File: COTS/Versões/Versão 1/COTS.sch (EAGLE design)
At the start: 12 parts

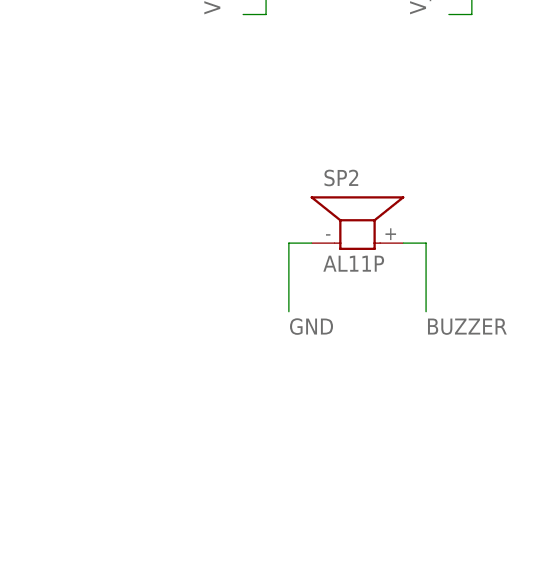
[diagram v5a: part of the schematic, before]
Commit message: CHORE: colocando  pads ovais
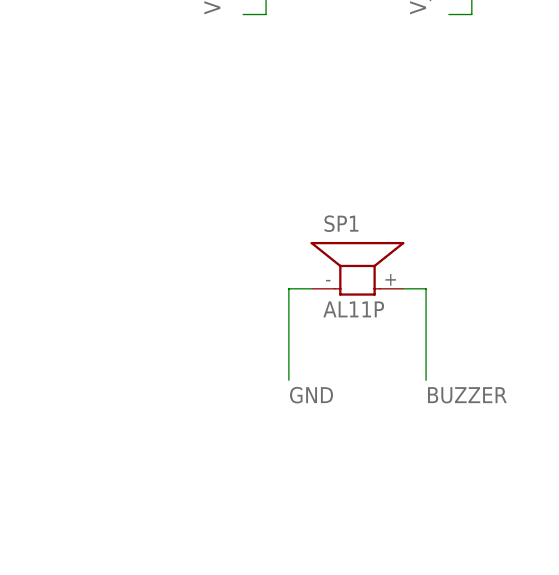
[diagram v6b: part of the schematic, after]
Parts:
- removed SP2: AL11P, buzzer:AL11P
- added SP1: AL11P, buzzer:AL11P
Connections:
- net BUZZER: now also SP1.2; no longer SP2.2
- net GND: now also SP1.1; no longer SP2.1
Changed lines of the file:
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@@
 <drawing>
 <settings>
-<setting alwaysvectorfont="yes"/>
+<setting alwaysvectorfont="no"/>
 <setting verticaltext="up"/>
 </settings>
@@
 </classes>
 <parts>
-<part name="U$1" library="CRD" library_urn="urn:adsk.eagle:library:39051337" deviceset="MPU6050" device="V1" package3d_urn="urn:adsk.eagle:package:39029071/8" override_package3d_urn="urn:adsk.eagle:package:49473311/2" override_package_urn="urn:adsk.eagle:footprint:39029067/6"/>
-<part name="U$2" library="ESP32-DEVKITV1" library_urn="urn:adsk.eagle:library:44018017" deviceset="ESP32DEVKITV1" device="" package3d_urn="urn:adsk.eagle:package:44018021/1" override_package3d_urn="urn:adsk.eagle:package:44018021/2" override_package_urn="urn:adsk.eagle:footprint:44018019/1"/>
-<part name="U$3" library="CRD" library_urn="urn:adsk.eagle:library:39051337" deviceset="BMP390" device="V1" package3d_urn="urn:adsk.eagle:package:40965124/5" override_package3d_urn="urn:adsk.eagle:package:49473309/2" override_package_urn="urn:adsk.eagle:footprint:40965120/5"/>
-<part name="U$4" library="CRD" library_urn="urn:adsk.eagle:library:39051337" deviceset="JST2.54X2P" device="" package3d_urn="urn:adsk.eagle:package:39191967/2" override_package3d_urn="urn:adsk.eagle:package:49473313/2" override_package_urn="urn:adsk.eagle:footprint:39191965/1"/>
-<part name="U$5" library="CRD" library_urn="urn:adsk.eagle:library:39051337" deviceset="JST2.54X2P" device="" package3d_urn="urn:adsk.eagle:package:39191967/2"/>
-<part name="U$6" library="CRD" library_urn="urn:adsk.eagle:library:39051337" deviceset="JST2.54X2P" device="" package3d_urn="urn:adsk.eagle:package:39191967/2"/>
-<part name="U$7" library="CRD" library_urn="urn:adsk.eagle:library:39051337" deviceset="JST2.54X2P" device="" package3d_urn="urn:adsk.eagle:package:39191967/2"/>
-<part name="U$9" library="CRD" library_urn="urn:adsk.eagle:library:39051337" deviceset="JST2.54X2P" device="" package3d_urn="urn:adsk.eagle:package:39191967/2"/>
-<part name="SP2" library="buzzer" library_urn="urn:adsk.eagle:library:113" deviceset="AL11P" device="" package3d_urn="urn:adsk.eagle:package:5308/1" override_package3d_urn="urn:adsk.eagle:package:49481862/2" override_package_urn="urn:adsk.eagle:footprint:5250/1"/>
+<part name="U$1" library="CRD" library_urn="urn:adsk.eagle:library:39051337" deviceset="MPU6050" device="V1" package3d_urn="urn:adsk.eagle:package:39029071/10" override_package3d_urn="urn:adsk.eagle:package:49473311/2" override_package_urn="urn:adsk.eagle:footprint:39029067/6" override_locally_modified="yes"/>
+<part name="U$2" library="ESP32-DEVKITV1" library_urn="urn:adsk.eagle:library:44018017" deviceset="ESP32DEVKITV1" device="" package3d_urn="urn:adsk.eagle:package:44018021/2"/>
+<part name="U$3" library="CRD" library_urn="urn:adsk.eagle:library:39051337" deviceset="BMP390" device="V1" package3d_urn="urn:adsk.eagle:package:40965124/8" override_package3d_urn="urn:adsk.eagle:package:49473309/2" override_package_urn="urn:adsk.eagle:footprint:40965120/5" override_locally_modified="yes"/>
+<part name="U$4" library="CRD" library_urn="urn:adsk.eagle:library:39051337" deviceset="JST2.54X2P" device="" package3d_urn="urn:adsk.eagle:package:39191967/3" override_package3d_urn="urn:adsk.eagle:package:49473313/2" override_package_urn="urn:adsk.eagle:footprint:39191965/1" override_locally_modified="yes"/>
+<part name="U$5" library="CRD" library_urn="urn:adsk.eagle:library:39051337" deviceset="JST2.54X2P" device="" package3d_urn="urn:adsk.eagle:package:39191967/3"/>
+<part name="U$6" library="CRD" library_urn="urn:adsk.eagle:library:39051337" deviceset="JST2.54X2P" device="" package3d_urn="urn:adsk.eagle:package:39191967/3"/>
+<part name="U$7" library="CRD" library_urn="urn:adsk.eagle:library:39051337" deviceset="JST2.54X2P" device="" package3d_urn="urn:adsk.eagle:package:39191967/3"/>
+<part name="U$9" library="CRD" library_urn="urn:adsk.eagle:library:39051337" deviceset="JST2.54X2P" device="" package3d_urn="urn:adsk.eagle:package:39191967/3"/>
 <part name="IC1" library="v-reg" library_urn="urn:adsk.eagle:library:409" deviceset="78XXL" device="" package3d_urn="urn:adsk.eagle:package:30361/1" override_package3d_urn="urn:adsk.eagle:package:49481863/2" override_package_urn="urn:adsk.eagle:footprint:30303/1"/>
 <part name="U$8" library="CRD" library_urn="urn:adsk.eagle:library:39051337" deviceset="CHAVE_SS-5GL" device="" package3d_urn="urn:adsk.eagle:package:45208058/14"/>
-<part name="U$10" library="CRD" library_urn="urn:adsk.eagle:library:39051337" deviceset="BMP280" device="V1" package3d_urn="urn:adsk.eagle:package:39029072/6"/>
+<part name="U$10" library="CRD" library_urn="urn:adsk.eagle:library:39051337" deviceset="BMP280" device="V1" package3d_urn="urn:adsk.eagle:package:39029072/8"/>
+<part name="SP1" library="buzzer" deviceset="AL11P" device="" package3d_urn="urn:adsk.eagle:package:5308/1"/>
 </parts>
 <sheets>
@@
 <instance part="U$7" gate="G$1" x="60.96" y="116.84" smashed="yes"/>
 <instance part="U$9" gate="G$1" x="-73.66" y="116.84" smashed="yes"/>
-<instance part="SP2" gate="G$1" x="236.22" y="53.34" smashed="yes">
-<attribute name="NAME" x="232.41" y="59.69" size="1.778" layer="95"/>
-<attribute name="VALUE" x="232.41" y="50.165" size="1.778" layer="96"/>
-</instance>
 <instance part="IC1" gate="A" x="-35.56" y="68.58" smashed="yes">
 <attribute name="NAME" x="-33.02" y="60.96" size="1.778" layer="95"/>
@@
 <instance part="U$8" gate="G$1" x="236.22" y="101.6" smashed="yes"/>
 <instance part="U$10" gate="G$1" x="88.9" y="5.08" smashed="yes"/>
+<instance part="SP1" gate="G$1" x="236.22" y="48.26" smashed="yes">
+<attribute name="NAME" x="232.41" y="54.61" size="1.778" layer="95"/>
+<attribute name="VALUE" x="232.41" y="45.085" size="1.778" layer="96"/>
+</instance>
 </instances>
 <busses>
@@
 </segment>
 <segment>
-<pinref part="SP2" gate="G$1" pin="1"/>
-<wire x1="231.14" y1="53.34" x2="228.6" y2="53.34" width="0.1524" layer="91"/>
-<wire x1="228.6" y1="53.34" x2="228.6" y2="45.72" width="0.1524" layer="91"/>
-<label x="228.6" y="43.18" size="1.778" layer="95"/>
-</segment>
-<segment>
 <pinref part="IC1" gate="A" pin="GND"/>
 <wire x1="-35.56" y1="60.96" x2="-35.56" y2="55.88" width="0.1524" layer="91"/>
@@
 <label x="81.28" y="-20.32" size="1.778" layer="95" rot="R90"/>
 </segment>
+<segment>
+<pinref part="SP1" gate="G$1" pin="1"/>
+<wire x1="231.14" y1="48.26" x2="228.6" y2="48.26" width="0.1524" layer="91"/>
+<wire x1="228.6" y1="48.26" x2="228.6" y2="38.1" width="0.1524" layer="91"/>
+<label x="228.6" y="35.56" size="1.778" layer="95"/>
+</segment>
 </net>
 <net name="SKIB1" class="0">
@@
 <net name="BUZZER" class="0">
 <segment>
-<pinref part="SP2" gate="G$1" pin="2"/>
-<wire x1="241.3" y1="53.34" x2="243.84" y2="53.34" width="0.1524" layer="91"/>
-<wire x1="243.84" y1="53.34" x2="243.84" y2="45.72" width="0.1524" layer="91"/>
-<label x="243.84" y="43.18" size="1.778" layer="95"/>
-</segment>
-<segment>
 <pinref part="U$2" gate="G$1" pin="IO14"/>
 <wire x1="83.82" y1="40.64" x2="73.66" y2="40.64" width="0.1524" layer="91"/>
 <label x="73.66" y="40.64" size="1.778" layer="95"/>
 </segment>
-</net>
+<segment>
+<pinref part="SP1" gate="G$1" pin="2"/>
+<wire x1="241.3" y1="48.26" x2="243.84" y2="48.26" width="0.1524" layer="91"/>
+<wire x1="243.84" y1="48.26" x2="243.84" y2="38.1" width="0.1524" layer="91"/>
+<label x="243.84" y="35.56" size="1.778" layer="95"/>
+</segment>
+</net>
